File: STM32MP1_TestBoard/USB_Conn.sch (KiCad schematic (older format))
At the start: 4 parts

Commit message: updated bom, readme
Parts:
- J13: renamed from J?; Mfr (none) -> XKB; PartNo (none) -> U262-161N-4BVC11
- J14: renamed from J?; footprint (none) -> Connector_USB:USB_A_Molex_67643_Horizontal; Mfr (none) -> Molex; PartNo (none) -> 676432911
- gave numbers to parts that had none: 2
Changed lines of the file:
@@
 $EndDescr
 $Comp
-L Connector:USB_C_Receptacle J?
+L Connector:USB_C_Receptacle J13
 U 1 1 611068DF
 P 4700 2350
-F 0 "J?" H 4807 3617 50  0000 C CNN
+F 0 "J13" H 4807 3617 50  0000 C CNN
 F 1 "USB_C_Receptacle" H 4807 3526 50  0000 C CNN
 F 2 "Connector_USB:USB_C_Receptacle_XKB_U262-16XN-4BVC11" H 4850 2350 50  0001 C CNN
 F 3 "https://www.usb.org/sites/default/files/documents/usb_type-c.zip" H 4850 2350 50  0001 C CNN
+F 4 "XKB" H 4700 2350 50  0001 C CNN "Mfr"
+F 5 "U262-161N-4BVC11" H 4700 2350 50  0001 C CNN "PartNo"
 	1    4700 2350
 	1    0    0    -1
@@
 	5575 2050 5300 2050
 $Comp
-L Device:R R?
+L Device:R R50
 U 1 1 611068EF
 P 5600 1550
-F 0 "R?" V 5525 1550 50  0000 C CNN
+F 0 "R50" V 5525 1550 50  0000 C CNN
 F 1 "5K1" V 5600 1550 50  0000 C CNN
 F 2 "Resistor_SMD:R_0402_1005Metric_Pad0.72x0.64mm_HandSolder" V 5530 1550 50  0001 C CNN
 F 3 "~" H 5600 1550 50  0001 C CNN
+F 4 "~" H 5600 1550 50  0001 C CNN "Mfr"
+F 5 "~" H 5600 1550 50  0001 C CNN "PartNo"
 	1    5600 1550
 	0    1    1    0
 $EndComp
 $Comp
-L Device:R R?
+L Device:R R51
 U 1 1 611068F5
 P 5600 1650
-F 0 "R?" V 5675 1650 50  0000 C CNN
+F 0 "R51" V 5675 1650 50  0000 C CNN
 F 1 "5K1" V 5600 1650 50  0000 C CNN
 F 2 "Resistor_SMD:R_0402_1005Metric_Pad0.72x0.64mm_HandSolder" V 5530 1650 50  0001 C CNN
 F 3 "~" H 5600 1650 50  0001 C CNN
+F 4 "~" H 5600 1650 50  0001 C CNN "Mfr"
+F 5 "~" H 5600 1650 50  0001 C CNN "PartNo"
 	1    5600 1650
 	0    1    1    0
@@
 	5950 1550 5950 1650
 $Comp
-L power:GNDS #PWR?
+L power:GNDS #PWR0128
 U 1 1 611068FF
 P 5950 1675
-F 0 "#PWR?" H 5950 1425 50  0001 C CNN
+F 0 "#PWR0128" H 5950 1425 50  0001 C CNN
 F 1 "GNDS" H 6100 1675 50  0000 C CNN
 F 2 "" H 5950 1675 50  0001 C CNN
@@
 	5550 1350 5550 1025
 $Comp
-L power:+5V #PWR?
+L power:+5V #PWR0129
 U 1 1 6110690A
 P 5550 1025
-F 0 "#PWR?" H 5550 875 50  0001 C CNN
+F 0 "#PWR0129" H 5550 875 50  0001 C CNN
 F 1 "+5V" H 5565 1198 50  0000 C CNN
 F 2 "" H 5550 1025 50  0001 C CNN
@@
 	4700 3950 4700 4350
 $Comp
-L power:GNDS #PWR?
+L power:GNDS #PWR0130
 U 1 1 61106911
 P 4700 4350
-F 0 "#PWR?" H 4700 4100 50  0001 C CNN
+F 0 "#PWR0130" H 4700 4100 50  0001 C CNN
 F 1 "GNDS" H 4705 4177 50  0000 C CNN
 F 2 "" H 4700 4350 50  0001 C CNN
@@
 $EndComp
 $Comp
-L Connector:USB_A J?
+L Connector:USB_A J14
 U 1 1 61106917
 P 4725 5775
-F 0 "J?" H 4782 6242 50  0000 C CNN
+F 0 "J14" H 4782 6242 50  0000 C CNN
 F 1 "USB_A" H 4782 6151 50  0000 C CNN
-F 2 "" H 4875 5725 50  0001 C CNN
-F 3 " ~" H 4875 5725 50  0001 C CNN
+F 2 "Connector_USB:USB_A_Molex_67643_Horizontal" H 4875 5725 50  0001 C CNN
+F 3 " https://www.molex.com/webdocs/datasheets/pdf/en-us/0676432911_IO_CONNECTORS.pdf" H 4875 5725 50  0001 C CNN
+F 4 "Molex" H 4725 5775 50  0001 C CNN "Mfr"
+F 5 "676432911" H 4725 5775 50  0001 C CNN "PartNo"
 	1    4725 5775
 	1    0    0    -1
 $EndComp
 Wire Wire Line
-	5025 5575 5500 5575
+	5025 5575 5300 5575
 Wire Wire Line
 	5500 5575 5500 5150
 $Comp
-L power:+5V #PWR?
+L power:+5V #PWR0131
 U 1 1 6110691F
 P 5500 5150
-F 0 "#PWR?" H 5500 5000 50  0001 C CNN
+F 0 "#PWR0131" H 5500 5000 50  0001 C CNN
 F 1 "+5V" H 5515 5323 50  0000 C CNN
 F 2 "" H 5500 5150 50  0001 C CNN
@@
 	4725 6175 4725 6450
 $Comp
-L power:GNDS #PWR?
+L power:GNDS #PWR0132
 U 1 1 61106928
 P 4725 6450
-F 0 "#PWR?" H 4725 6200 50  0001 C CNN
+F 0 "#PWR0132" H 4725 6200 50  0001 C CNN
 F 1 "GNDS" H 4730 6277 50  0000 C CNN
 F 2 "" H 4725 6450 50  0001 C CNN
@@
 Text HLabel 5500 5875 2    50   Input ~ 0
 USBA_DM
+$Comp
+L power:PWR_FLAG #FLG?
+U 1 1 603103FE
+P 5300 5575
+AR Path="/5FBD70AB/603103FE" Ref="#FLG?"  Part="1"
+AR Path="/6044C48A/603103FE" Ref="#FLG?"  Part="1"
+AR Path="/610FE7C3/603103FE" Ref="#FLG0112"  Part="1"
+F 0 "#FLG0112" H 5300 5650 50  0001 C CNN
+F 1 "PWR_FLAG" H 5300 5748 50  0001 C CNN
+F 2 "" H 5300 5575 50  0001 C CNN
+F 3 "~" H 5300 5575 50  0001 C CNN
+	1    5300 5575
+	1    0    0    -1
+$EndComp
+Connection ~ 5300 5575
+Wire Wire Line
+	5300 5575 5500 5575
 $EndSCHEMATC

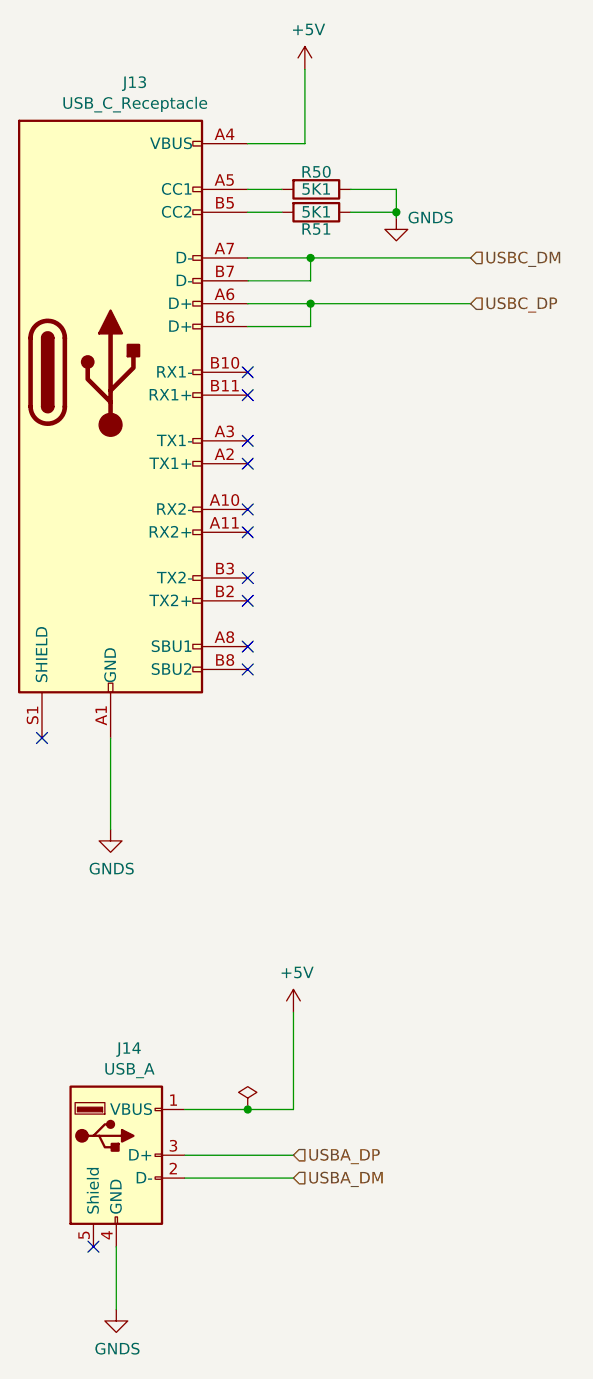
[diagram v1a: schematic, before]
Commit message: updated schematic design
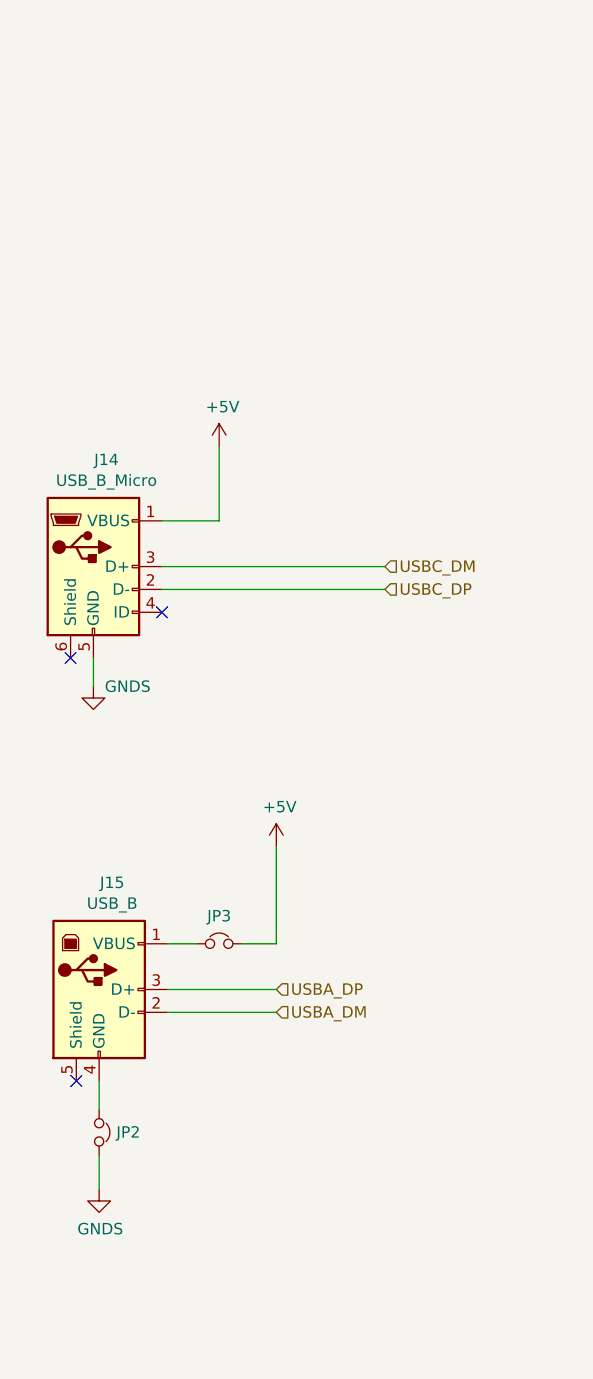
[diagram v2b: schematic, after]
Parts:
- removed J13: USB_C_Receptacle, Connector_USB:USB_C_Receptacle_XKB_U262-16XN-4BVC11, symbol Connector:USB_C_Receptacle
- removed J14: USB_A, Connector_USB:USB_A_Molex_67643_Horizontal, symbol Connector:USB_A
- removed R50, R51: 5K1, Resistor_SMD:R_0402_1005Metric_Pad0.72x0.64mm_HandSolder, symbol Device:R
- added J13: USB_B_Micro, Connector_USB:USB_Micro-B_Molex-105017-0001, symbol Connector:USB_B_Micro
- added J14: USB_B, Connector_USB:USB_B_Lumberg_2411_02_Horizontal, symbol Connector:USB_B
- added JP2, JP3: Jumper_NC_Small, Jumper:SolderJumper-2_P1.3mm_Bridged_Pad1.0x1.5mm, symbol Device:Jumper_NC_Small
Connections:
- net +5V: now also J13.1 (VBUS), JP2.2
- net GNDS: now also J13.5 (GND), JP3.2
- net USBA_DM: now also J14.2 (D-)
- net USBA_DP: now also J14.3 (D+)
- net USBC_DM: now also J13.3 (D+)
- net USBC_DP: now also J13.2 (D-)
- new net: J14.1 (VBUS), JP2.1
- new net: J14.4 (GND), JP3.1
- no-connect marks 12 -> 3
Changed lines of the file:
@@
 $Descr A4 11693 8268
 encoding utf-8
-Sheet 9 9
+Sheet 9 10
 Title ""
 Date ""
@@
 $EndDescr
 $Comp
-L Connector:USB_C_Receptacle J13
-U 1 1 611068DF
-P 4700 2350
-F 0 "J13" H 4807 3617 50  0000 C CNN
-F 1 "USB_C_Receptacle" H 4807 3526 50  0000 C CNN
-F 2 "Connector_USB:USB_C_Receptacle_XKB_U262-16XN-4BVC11" H 4850 2350 50  0001 C CNN
-F 3 "https://www.usb.org/sites/default/files/documents/usb_type-c.zip" H 4850 2350 50  0001 C CNN
-F 4 "XKB" H 4700 2350 50  0001 C CNN "Mfr"
-F 5 "U262-161N-4BVC11" H 4700 2350 50  0001 C CNN "PartNo"
-	1    4700 2350
+L power:GNDS #PWR0128
+U 1 1 611068FF
+P 4625 3725
+AR Path="/610FE7C3/611068FF" Ref="#PWR0128"  Part="1"
+AR Path="/6097C138/609989A6/611068FF" Ref="#PWR047"  Part="1"
+F 0 "#PWR047" H 4625 3475 50  0001 C CNN
+F 1 "GNDS" H 4775 3725 50  0000 C CNN
+F 2 "" H 4625 3725 50  0001 C CNN
+F 3 "" H 4625 3725 50  0001 C CNN
+	1    4625 3725
 	1    0    0    -1
 $EndComp
 Wire Wire Line
-	5300 1850 5575 1850
+	4925 3000 5175 3000
 Wire Wire Line
-	5575 1850 5575 1950
+	5175 3000 5175 2675
+$Comp
+L power:+5V #PWR0129
+U 1 1 6110690A
+P 5175 2675
+AR Path="/610FE7C3/6110690A" Ref="#PWR0129"  Part="1"
+AR Path="/6097C138/609989A6/6110690A" Ref="#PWR050"  Part="1"
+F 0 "#PWR050" H 5175 2525 50  0001 C CNN
+F 1 "+5V" H 5190 2848 50  0000 C CNN
+F 2 "" H 5175 2675 50  0001 C CNN
+F 3 "" H 5175 2675 50  0001 C CNN
+	1    5175 2675
+	1    0    0    -1
+$EndComp
 Wire Wire Line
-	5575 1950 5300 1950
+	5425 4850 5425 4425
+$Comp
+L power:+5V #PWR0131
+U 1 1 6110691F
+P 5425 4425
+AR Path="/610FE7C3/6110691F" Ref="#PWR0131"  Part="1"
+AR Path="/6097C138/609989A6/6110691F" Ref="#PWR051"  Part="1"
+F 0 "#PWR051" H 5425 4275 50  0001 C CNN
+F 1 "+5V" H 5440 4598 50  0000 C CNN
+F 2 "" H 5425 4425 50  0001 C CNN
+F 3 "" H 5425 4425 50  0001 C CNN
+	1    5425 4425
+	1    0    0    -1
+$EndComp
 Wire Wire Line
-	5575 1850 6275 1850
-Connection ~ 5575 1850
+	4950 5050 5425 5050
 Wire Wire Line
-	6275 2050 5575 2050
+	4950 5150 5425 5150
 Wire Wire Line
-	5300 2150 5575 2150
-Wire Wire Line
-	5575 2150 5575 2050
-Connection ~ 5575 2050
-Wire Wire Line
-	5575 2050 5300 2050
+	4650 5450 4650 5575
 $Comp
-L Device:R R50
-U 1 1 611068EF
-P 5600 1550
-F 0 "R50" V 5525 1550 50  0000 C CNN
-F 1 "5K1" V 5600 1550 50  0000 C CNN
-F 2 "Resistor_SMD:R_0402_1005Metric_Pad0.72x0.64mm_HandSolder" V 5530 1550 50  0001 C CNN
-F 3 "~" H 5600 1550 50  0001 C CNN
-F 4 "~" H 5600 1550 50  0001 C CNN "Mfr"
-F 5 "~" H 5600 1550 50  0001 C CNN "PartNo"
-	1    5600 1550
-	0    1    1    0
+L power:GNDS #PWR0132
+U 1 1 61106928
+P 4650 5925
+AR Path="/610FE7C3/61106928" Ref="#PWR0132"  Part="1"
+AR Path="/6097C138/609989A6/61106928" Ref="#PWR048"  Part="1"
+F 0 "#PWR048" H 4650 5675 50  0001 C CNN
+F 1 "GNDS" H 4655 5752 50  0000 C CNN
+F 2 "" H 4650 5925 50  0001 C CNN
+F 3 "" H 4650 5925 50  0001 C CNN
+	1    4650 5925
+	1    0    0    -1
+$EndComp
+NoConn ~ 4550 5450
+Text HLabel 5900 3200 2    50   Input ~ 0
+USBC_DM
+Text HLabel 5900 3300 2    50   Input ~ 0
+USBC_DP
+Text HLabel 5425 5050 2    50   Input ~ 0
+USBA_DP
+Text HLabel 5425 5150 2    50   Input ~ 0
+USBA_DM
+$Comp
+L Connector:USB_B_Micro J13
+U 1 1 5FC6FFE5
+P 4625 3200
+AR Path="/610FE7C3/5FC6FFE5" Ref="J13"  Part="1"
+AR Path="/6097C138/609989A6/5FC6FFE5" Ref="J14"  Part="1"
+F 0 "J14" H 4682 3667 50  0000 C CNN
+F 1 "USB_B_Micro" H 4682 3576 50  0000 C CNN
+F 2 "Connector_USB:USB_Micro-B_Molex-105017-0001" H 4775 3150 50  0001 C CNN
+F 3 "~" H 4775 3150 50  0001 C CNN
+	1    4625 3200
+	1    0    0    -1
 $EndComp
 $Comp
-L Device:R R51
-U 1 1 611068F5
-P 5600 1650
-F 0 "R51" V 5675 1650 50  0000 C CNN
-F 1 "5K1" V 5600 1650 50  0000 C CNN
-F 2 "Resistor_SMD:R_0402_1005Metric_Pad0.72x0.64mm_HandSolder" V 5530 1650 50  0001 C CNN
-F 3 "~" H 5600 1650 50  0001 C CNN
-F 4 "~" H 5600 1650 50  0001 C CNN "Mfr"
-F 5 "~" H 5600 1650 50  0001 C CNN "PartNo"
-	1    5600 1650
+L Connector:USB_B J14
+U 1 1 5FC70F47
+P 4650 5050
+AR Path="/610FE7C3/5FC70F47" Ref="J14"  Part="1"
+AR Path="/6097C138/609989A6/5FC70F47" Ref="J15"  Part="1"
+F 0 "J15" H 4707 5517 50  0000 C CNN
+F 1 "USB_B" H 4707 5426 50  0000 C CNN
+F 2 "Connector_USB:USB_B_Lumberg_2411_02_Horizontal" H 4800 5000 50  0001 C CNN
+F 3 " ~" H 4800 5000 50  0001 C CNN
+	1    4650 5050
+	1    0    0    -1
+$EndComp
+Wire Wire Line
+	4925 3200 5900 3200
+Wire Wire Line
+	4925 3300 5900 3300
+NoConn ~ 4925 3400
+NoConn ~ 4525 3600
+Wire Wire Line
+	4625 3600 4625 3725
+Wire Wire Line
+	4950 4850 5075 4850
+$Comp
+L Device:Jumper_NC_Small JP2
+U 1 1 5FC9168C
+P 5175 4850
+AR Path="/610FE7C3/5FC9168C" Ref="JP2"  Part="1"
+AR Path="/6097C138/609989A6/5FC9168C" Ref="JP3"  Part="1"
+F 0 "JP3" H 5175 4971 50  0000 C CNN
+F 1 "Jumper_NC_Small" H 5175 4971 50  0001 C CNN
+F 2 "Jumper:SolderJumper-2_P1.3mm_Bridged_Pad1.0x1.5mm" H 5175 4850 50  0001 C CNN
+F 3 "~" H 5175 4850 50  0001 C CNN
+	1    5175 4850
+	1    0    0    -1
+$EndComp
+Wire Wire Line
+	5275 4850 5425 4850
+$Comp
+L Device:Jumper_NC_Small JP3
+U 1 1 5FC94550
+P 4650 5675
+AR Path="/610FE7C3/5FC94550" Ref="JP3"  Part="1"
+AR Path="/6097C138/609989A6/5FC94550" Ref="JP2"  Part="1"
+F 0 "JP2" V 4650 5750 50  0000 L CNN
+F 1 "Jumper_NC_Small" H 4650 5796 50  0001 C CNN
+F 2 "Jumper:SolderJumper-2_P1.3mm_Bridged_Pad1.0x1.5mm" H 4650 5675 50  0001 C CNN
+F 3 "~" H 4650 5675 50  0001 C CNN
+	1    4650 5675
 	0    1    1    0
 $EndComp
 Wire Wire Line
-	5300 1550 5450 1550
-Wire Wire Line
-	5450 1650 5300 1650
-Wire Wire Line
-	5750 1550 5950 1550
-Wire Wire Line
-	5950 1550 5950 1650
-$Comp
-L power:GNDS #PWR0128
-U 1 1 611068FF
-P 5950 1675
-F 0 "#PWR0128" H 5950 1425 50  0001 C CNN
-F 1 "GNDS" H 6100 1675 50  0000 C CNN
-F 2 "" H 5950 1675 50  0001 C CNN
-F 3 "" H 5950 1675 50  0001 C CNN
-	1    5950 1675
-	1    0    0    -1
-$EndComp
-Wire Wire Line
-	5750 1650 5950 1650
-Connection ~ 5950 1650
-Wire Wire Line
-	5950 1650 5950 1675
-Wire Wire Line
-	5300 1350 5550 1350
-Wire Wire Line
-	5550 1350 5550 1025
-$Comp
-L power:+5V #PWR0129
-U 1 1 6110690A
-P 5550 1025
-F 0 "#PWR0129" H 5550 875 50  0001 C CNN
-F 1 "+5V" H 5565 1198 50  0000 C CNN
-F 2 "" H 5550 1025 50  0001 C CNN
-F 3 "" H 5550 1025 50  0001 C CNN
-	1    5550 1025
-	1    0    0    -1
-$EndComp
-Wire Wire Line
-	4700 3950 4700 4350
-$Comp
-L power:GNDS #PWR0130
-U 1 1 61106911
-P 4700 4350
-F 0 "#PWR0130" H 4700 4100 50  0001 C CNN
-F 1 "GNDS" H 4705 4177 50  0000 C CNN
-F 2 "" H 4700 4350 50  0001 C CNN
-F 3 "" H 4700 4350 50  0001 C CNN
-	1    4700 4350
-	1    0    0    -1
-$EndComp
-$Comp
-L Connector:USB_A J14
-U 1 1 61106917
-P 4725 5775
-F 0 "J14" H 4782 6242 50  0000 C CNN
-F 1 "USB_A" H 4782 6151 50  0000 C CNN
-F 2 "Connector_USB:USB_A_Molex_67643_Horizontal" H 4875 5725 50  0001 C CNN
-F 3 " https://www.molex.com/webdocs/datasheets/pdf/en-us/0676432911_IO_CONNECTORS.pdf" H 4875 5725 50  0001 C CNN
-F 4 "Molex" H 4725 5775 50  0001 C CNN "Mfr"
-F 5 "676432911" H 4725 5775 50  0001 C CNN "PartNo"
-	1    4725 5775
-	1    0    0    -1
-$EndComp
-Wire Wire Line
-	5025 5575 5300 5575
-Wire Wire Line
-	5500 5575 5500 5150
-$Comp
-L power:+5V #PWR0131
-U 1 1 6110691F
-P 5500 5150
-F 0 "#PWR0131" H 5500 5000 50  0001 C CNN
-F 1 "+5V" H 5515 5323 50  0000 C CNN
-F 2 "" H 5500 5150 50  0001 C CNN
-F 3 "" H 5500 5150 50  0001 C CNN
-	1    5500 5150
-	1    0    0    -1
-$EndComp
-Wire Wire Line
-	5025 5775 5500 5775
-Wire Wire Line
-	5025 5875 5500 5875
-Wire Wire Line
-	4725 6175 4725 6450
-$Comp
-L power:GNDS #PWR0132
-U 1 1 61106928
-P 4725 6450
-F 0 "#PWR0132" H 4725 6200 50  0001 C CNN
-F 1 "GNDS" H 4730 6277 50  0000 C CNN
-F 2 "" H 4725 6450 50  0001 C CNN
-F 3 "" H 4725 6450 50  0001 C CNN
-	1    4725 6450
-	1    0    0    -1
-$EndComp
-NoConn ~ 4625 6175
-NoConn ~ 4400 3950
-NoConn ~ 5300 2350
-NoConn ~ 5300 2450
-NoConn ~ 5300 2650
-NoConn ~ 5300 2750
-NoConn ~ 5300 2950
-NoConn ~ 5300 3050
-NoConn ~ 5300 3250
-NoConn ~ 5300 3350
-NoConn ~ 5300 3550
-NoConn ~ 5300 3650
-Text HLabel 6275 1850 2    50   Input ~ 0
-USBC_DM
-Text HLabel 6275 2050 2    50   Input ~ 0
-USBC_DP
-Text HLabel 5500 5775 2    50   Input ~ 0
-USBA_DP
-Text HLabel 5500 5875 2    50   Input ~ 0
-USBA_DM
-$Comp
-L power:PWR_FLAG #FLG?
-U 1 1 603103FE
-P 5300 5575
-AR Path="/5FBD70AB/603103FE" Ref="#FLG?"  Part="1"
-AR Path="/6044C48A/603103FE" Ref="#FLG?"  Part="1"
-AR Path="/610FE7C3/603103FE" Ref="#FLG0112"  Part="1"
-F 0 "#FLG0112" H 5300 5650 50  0001 C CNN
-F 1 "PWR_FLAG" H 5300 5748 50  0001 C CNN
-F 2 "" H 5300 5575 50  0001 C CNN
-F 3 "~" H 5300 5575 50  0001 C CNN
-	1    5300 5575
-	1    0    0    -1
-$EndComp
-Connection ~ 5300 5575
-Wire Wire Line
-	5300 5575 5500 5575
+	4650 5775 4650 5925
 $EndSCHEMATC

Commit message: layout update
backup. work in progress
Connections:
- net USBA_DM renamed USB_D2_N
- net USBA_DP renamed USB_D2_P
- net USBC_DM renamed USB_D1_N
- net USBC_DP renamed USB_D1_P
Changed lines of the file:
@@
 $Descr A4 11693 8268
 encoding utf-8
-Sheet 9 10
+Sheet 8 10
 Title ""
 Date ""
@@
 NoConn ~ 4550 5450
 Text HLabel 5900 3200 2    50   Input ~ 0
-USBC_DM
+USB_D1_N
 Text HLabel 5900 3300 2    50   Input ~ 0
-USBC_DP
+USB_D1_P
 Text HLabel 5425 5050 2    50   Input ~ 0
-USBA_DP
+USB_D2_P
 Text HLabel 5425 5150 2    50   Input ~ 0
-USBA_DM
+USB_D2_N
 $Comp
 L Connector:USB_B_Micro J13

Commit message: update
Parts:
- removed J14: USB_B, Connector_USB:USB_B_Lumberg_2411_02_Horizontal, symbol Connector:USB_B
- removed JP2, JP3: Jumper_NC_Small, Jumper:SolderJumper-2_P1.3mm_Bridged_Pad1.0x1.5mm, symbol Device:Jumper_NC_Small
- added J8: USB_B_Micro, Connector_USB:USB_Micro-B_Molex-105017-0001, symbol Connector:USB_B_Micro
- added R16, R17: 0R, Resistor_SMD:R_0402_1005Metric_Pad0.72x0.64mm_HandSolder, symbol Device:R
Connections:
- net +5V: now also R16.1
- net GNDS: now also R17.1
- net USB_D2_N: now also J8.2 (D-)
- net USB_D2_P: now also J8.3 (D+)
- new net: J8.1 (VBUS), R16.2
- new net: J8.5 (GND), R17.2
- no-connect marks 3 -> 4
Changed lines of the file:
@@
 Wire Wire Line
 	4950 5150 5425 5150
-Wire Wire Line
-	4650 5450 4650 5575
 $Comp
 L power:GNDS #PWR0132
@@
 	1    0    0    -1
 $EndComp
-$Comp
-L Connector:USB_B J14
-U 1 1 5FC70F47
-P 4650 5050
-AR Path="/610FE7C3/5FC70F47" Ref="J14"  Part="1"
-AR Path="/6097C138/609989A6/5FC70F47" Ref="J15"  Part="1"
-F 0 "J15" H 4707 5517 50  0000 C CNN
-F 1 "USB_B" H 4707 5426 50  0000 C CNN
-F 2 "Connector_USB:USB_B_Lumberg_2411_02_Horizontal" H 4800 5000 50  0001 C CNN
-F 3 " ~" H 4800 5000 50  0001 C CNN
-	1    4650 5050
-	1    0    0    -1
-$EndComp
 Wire Wire Line
 	4925 3200 5900 3200
@@
 Wire Wire Line
 	4625 3600 4625 3725
-Wire Wire Line
-	4950 4850 5075 4850
 $Comp
-L Device:Jumper_NC_Small JP2
-U 1 1 5FC9168C
-P 5175 4850
-AR Path="/610FE7C3/5FC9168C" Ref="JP2"  Part="1"
-AR Path="/6097C138/609989A6/5FC9168C" Ref="JP3"  Part="1"
-F 0 "JP3" H 5175 4971 50  0000 C CNN
-F 1 "Jumper_NC_Small" H 5175 4971 50  0001 C CNN
-F 2 "Jumper:SolderJumper-2_P1.3mm_Bridged_Pad1.0x1.5mm" H 5175 4850 50  0001 C CNN
-F 3 "~" H 5175 4850 50  0001 C CNN
-	1    5175 4850
+L Connector:USB_B_Micro J?
+U 1 1 5FC689D6
+P 4650 5050
+AR Path="/610FE7C3/5FC689D6" Ref="J?"  Part="1"
+AR Path="/6097C138/609989A6/5FC689D6" Ref="J8"  Part="1"
+F 0 "J8" H 4707 5517 50  0000 C CNN
+F 1 "USB_B_Micro" H 4707 5426 50  0000 C CNN
+F 2 "Connector_USB:USB_Micro-B_Molex-105017-0001" H 4800 5000 50  0001 C CNN
+F 3 "~" H 4800 5000 50  0001 C CNN
+	1    4650 5050
 	1    0    0    -1
 $EndComp
+NoConn ~ 4950 5250
 Wire Wire Line
-	5275 4850 5425 4850
+	4950 4850 5050 4850
+Wire Wire Line
+	4650 5450 4650 5575
 $Comp
-L Device:Jumper_NC_Small JP3
-U 1 1 5FC94550
-P 4650 5675
-AR Path="/610FE7C3/5FC94550" Ref="JP3"  Part="1"
-AR Path="/6097C138/609989A6/5FC94550" Ref="JP2"  Part="1"
-F 0 "JP2" V 4650 5750 50  0000 L CNN
-F 1 "Jumper_NC_Small" H 4650 5796 50  0001 C CNN
-F 2 "Jumper:SolderJumper-2_P1.3mm_Bridged_Pad1.0x1.5mm" H 4650 5675 50  0001 C CNN
-F 3 "~" H 4650 5675 50  0001 C CNN
-	1    4650 5675
+L Device:R R16
+U 1 1 5FC7250A
+P 5200 4850
+F 0 "R16" V 4993 4850 50  0000 C CNN
+F 1 "0R" V 5084 4850 50  0000 C CNN
+F 2 "Resistor_SMD:R_0402_1005Metric_Pad0.72x0.64mm_HandSolder" V 5130 4850 50  0001 C CNN
+F 3 "~" H 5200 4850 50  0001 C CNN
+	1    5200 4850
 	0    1    1    0
 $EndComp
 Wire Wire Line
-	4650 5775 4650 5925
+	5350 4850 5425 4850
+$Comp
+L Device:R R17
+U 1 1 5FC752AF
+P 4650 5725
+F 0 "R17" H 4580 5679 50  0000 R CNN
+F 1 "0R" H 4580 5770 50  0000 R CNN
+F 2 "Resistor_SMD:R_0402_1005Metric_Pad0.72x0.64mm_HandSolder" V 4580 5725 50  0001 C CNN
+F 3 "~" H 4650 5725 50  0001 C CNN
+	1    4650 5725
+	-1   0    0    1
+$EndComp
+Wire Wire Line
+	4650 5875 4650 5925
 $EndSCHEMATC
